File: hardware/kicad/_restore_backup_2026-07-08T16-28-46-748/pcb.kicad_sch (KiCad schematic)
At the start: 7 parts, among them J1 ENCODER, J2 MOTOR, J3 12V MOTOR, U1 Dual_L298N_H_Bridge

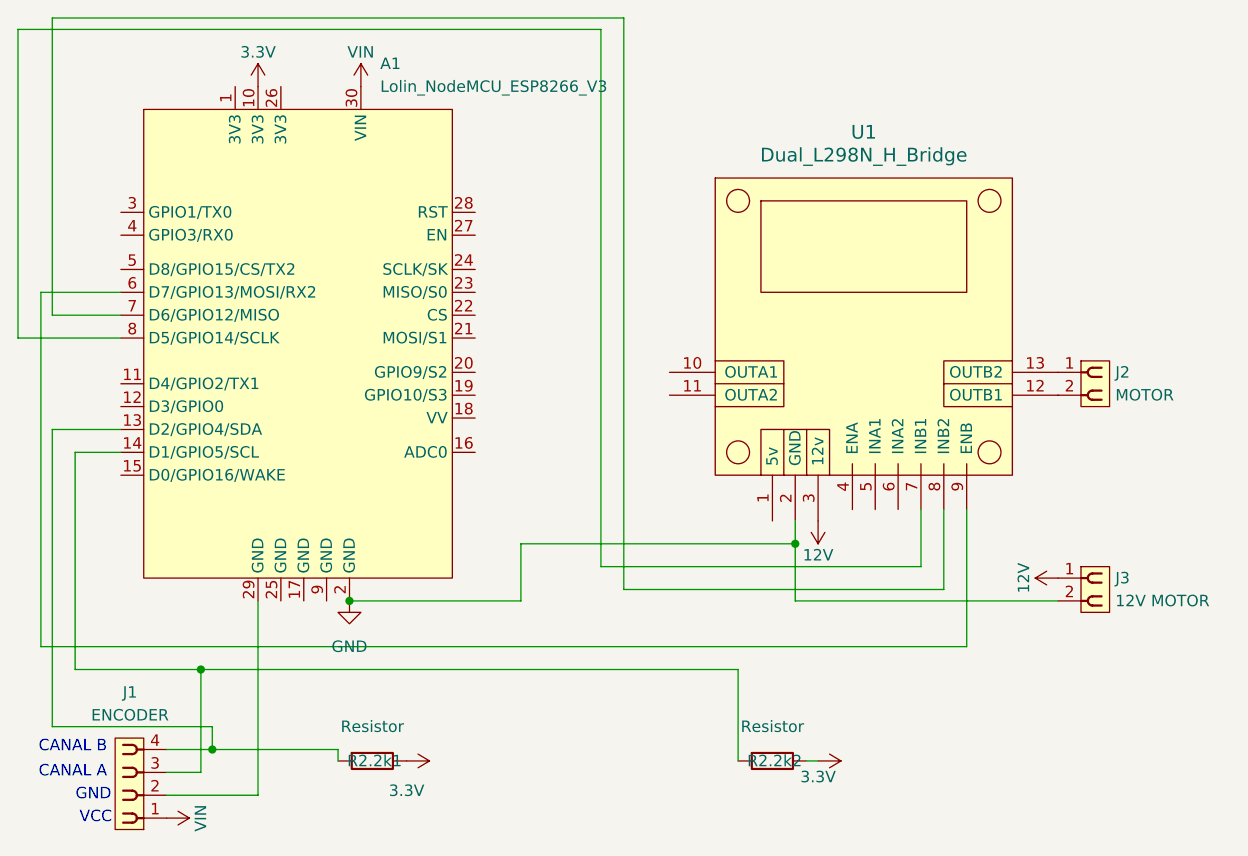
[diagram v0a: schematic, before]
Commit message: fix:tirando o divisor de tensão e adcionando a forma correta de leitura do encoder
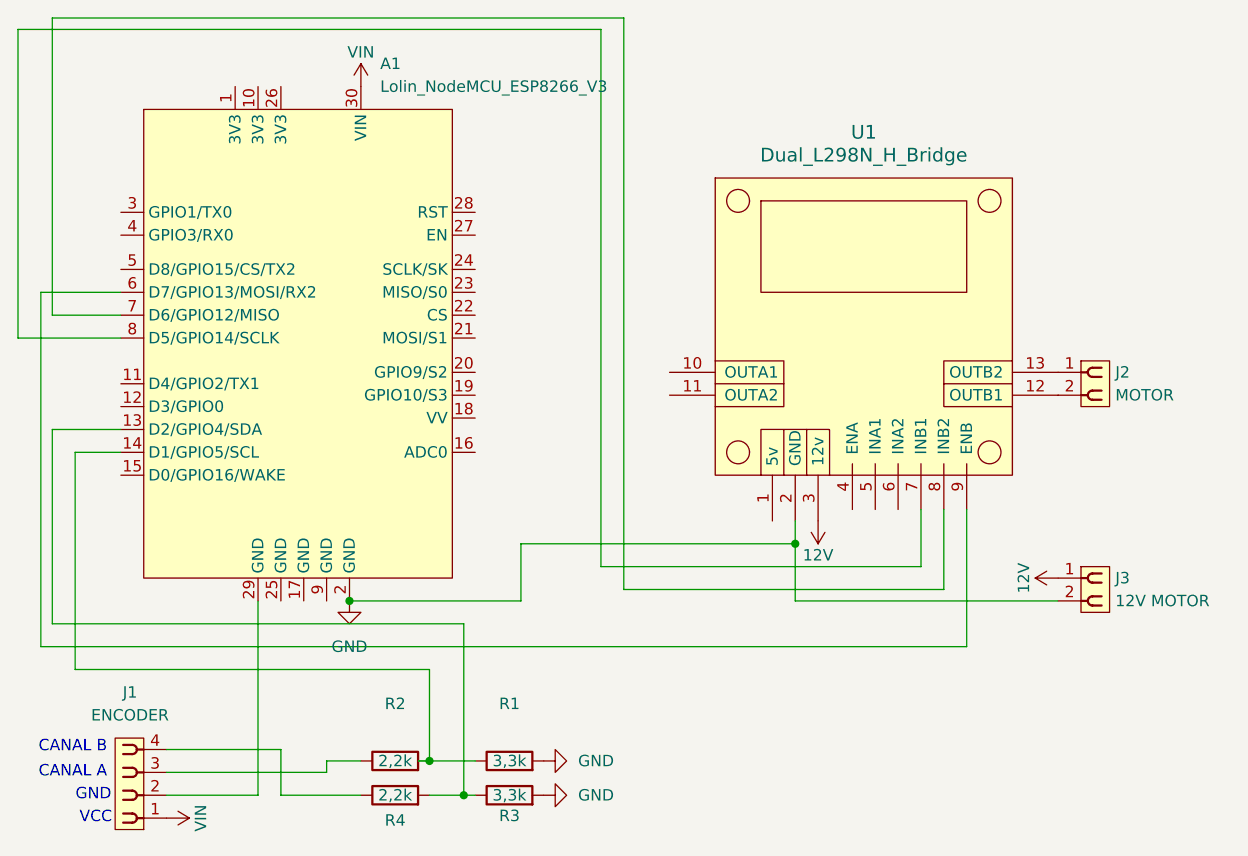
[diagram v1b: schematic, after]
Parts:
- removed R2.2k1, R2.2k2: Resistor, Resistor_THT:R_Axial_DIN0207_L6.3mm_D2.5mm_P10.16mm_Horizontal, symbol PCM_SL_Devices:Resistor
- added R1, R3: 3,3k, Resistor_THT:R_Axial_DIN0207_L6.3mm_D2.5mm_P10.16mm_Horizontal, symbol Device:R
- added R2, R4: 2,2k, Resistor_THT:R_Axial_DIN0207_L6.3mm_D2.5mm_P10.16mm_Horizontal, symbol Device:R
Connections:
- net GND: now also R1.2, R3.2
- net at J1.3: now also R2.1; no longer A1.14 (D1/GPIO5/SCL)
- net at J1.4: now also R4.1; no longer A1.13 (D2/GPIO4/SDA)
- net 3.3V: no longer names the net of A1.10 (3V3)
- new net: A1.13 (D2/GPIO4/SDA), R3.1, R4.2
- new net: A1.14 (D1/GPIO5/SCL), R1.1, R2.2
